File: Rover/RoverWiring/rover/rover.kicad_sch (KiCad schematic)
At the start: 6 parts, among them U1 HC-SR04_Ultrasonic_Sensor, U2 HC-SR04_Ultrasonic_Sensor

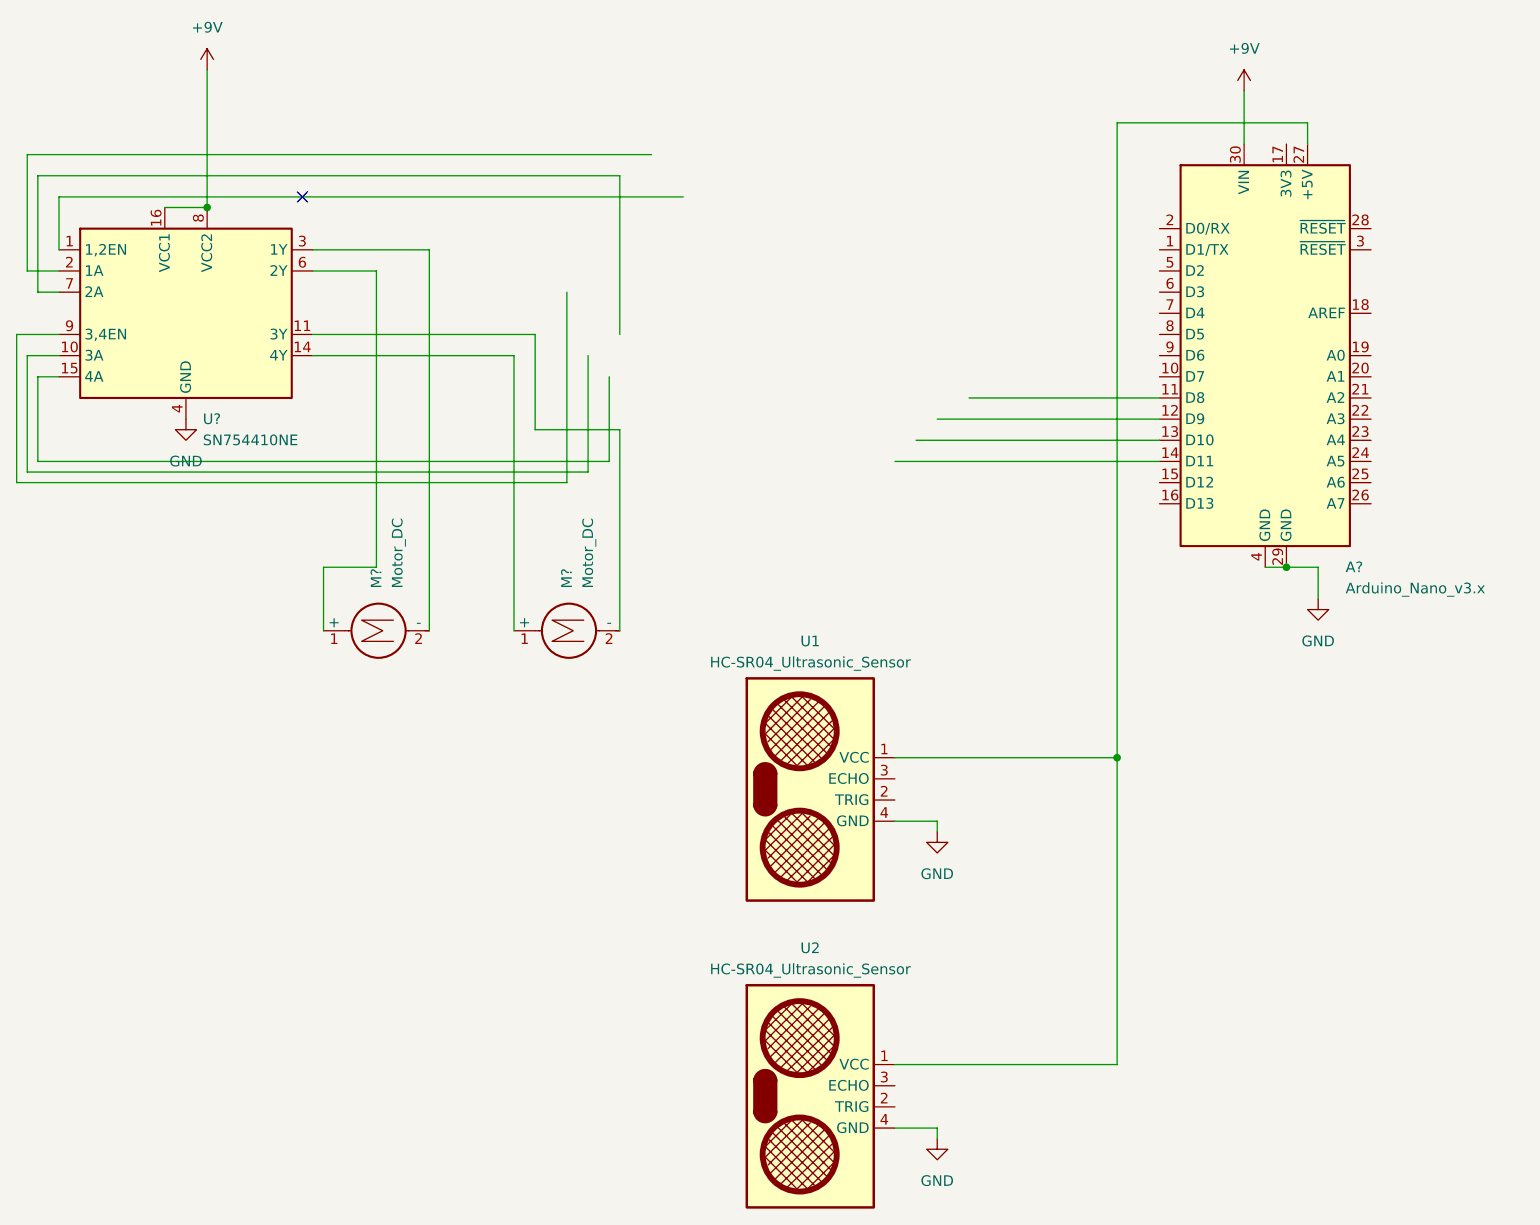
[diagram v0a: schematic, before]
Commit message: Fixed Calibration and added code to counter the issue of a diagonal wall anti collision
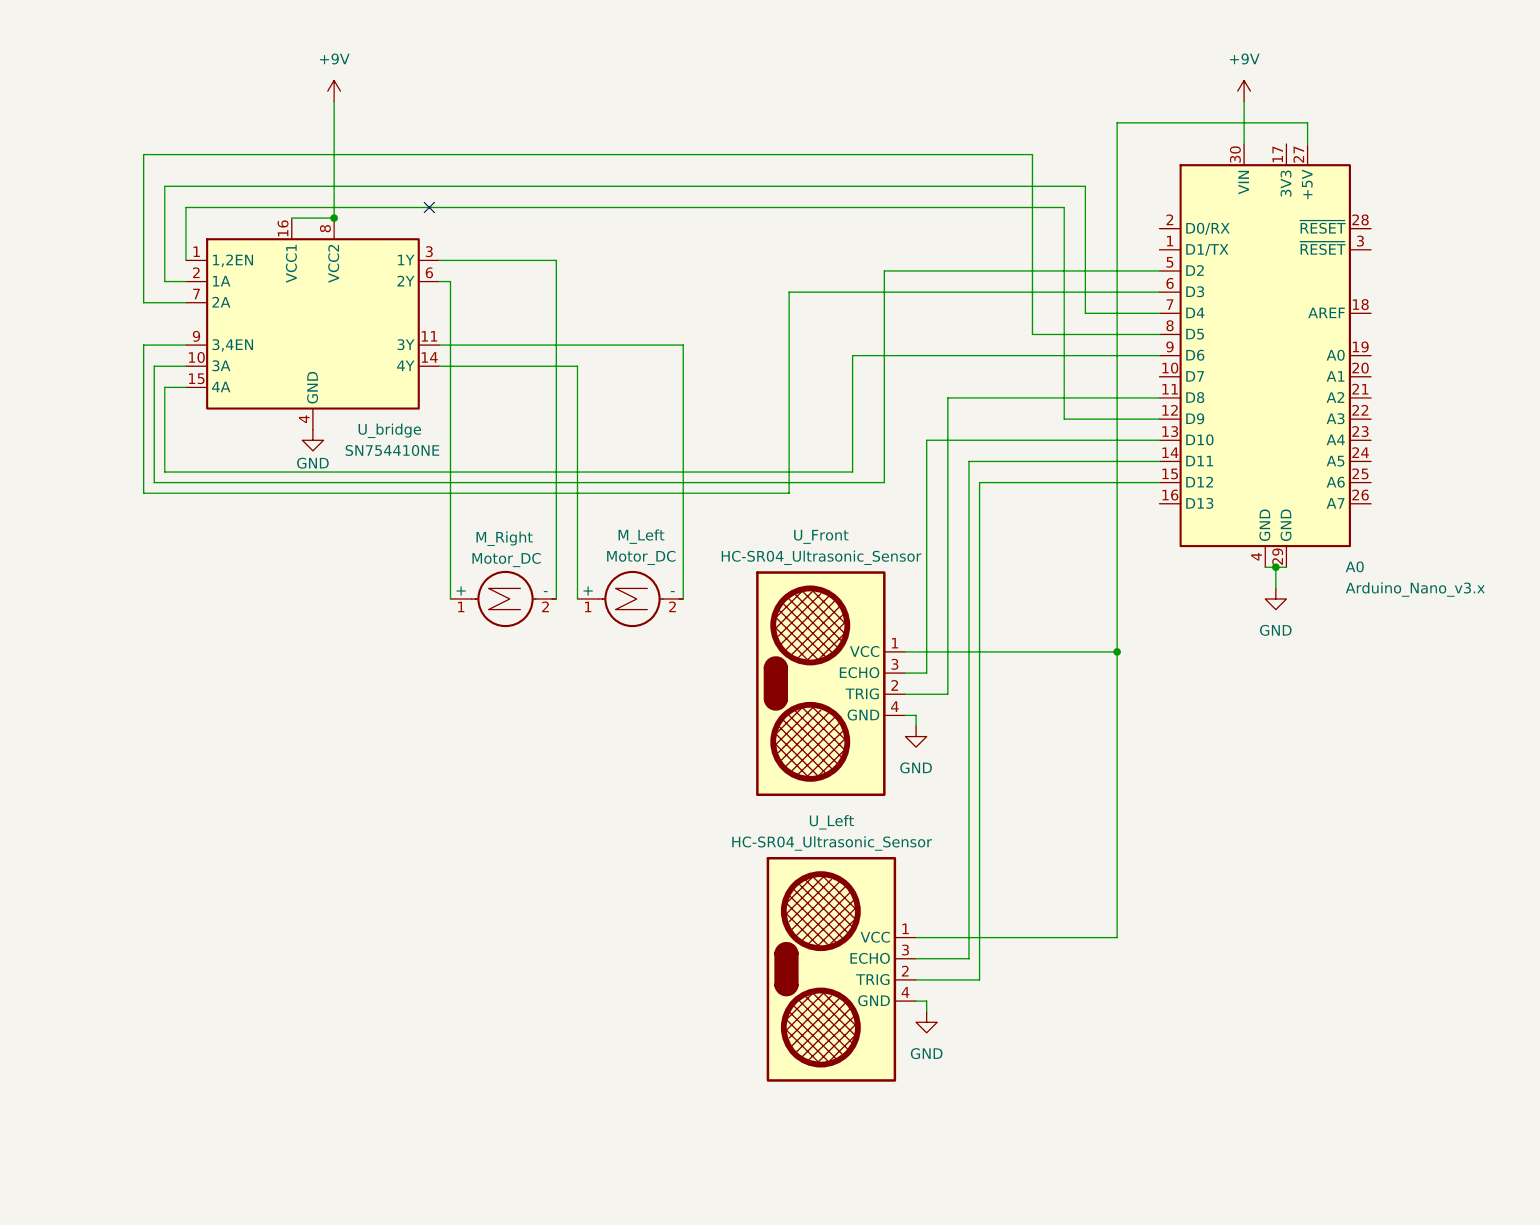
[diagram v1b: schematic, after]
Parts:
- gave numbers to parts that had none: 4
- renumbered U1 to U_Front, U2 to U_Left
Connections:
- net at U_bridge.1 (1,2EN): now also A0.12 (D9)
- net at U_bridge.10 (3A): now also A0.5 (D2)
- net at U_bridge.15 (4A): now also A0.9 (D6)
- net at U_bridge.2 (1A): now also A0.7 (D4)
- net at U_bridge.7 (2A): now also A0.8 (D5)
- net at U_bridge.9 (3,4EN): now also A0.6 (D3)
- net at A0.11 (D8): now also U_Front.2 (TRIG)
- net at A0.13 (D10): now also U_Front.3 (ECHO)
- net at A0.14 (D11): now also U_Left.3 (ECHO)
- net at A0.15 (D12): now also U_Left.2 (TRIG)
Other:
- moved on the sheet: M_Left, M_Right, U_Front, U_Left, U_bridge
